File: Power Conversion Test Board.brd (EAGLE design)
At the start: 136.7 x 125.3 mm, 48 parts, among them U1 LM2678, U2 LM2678

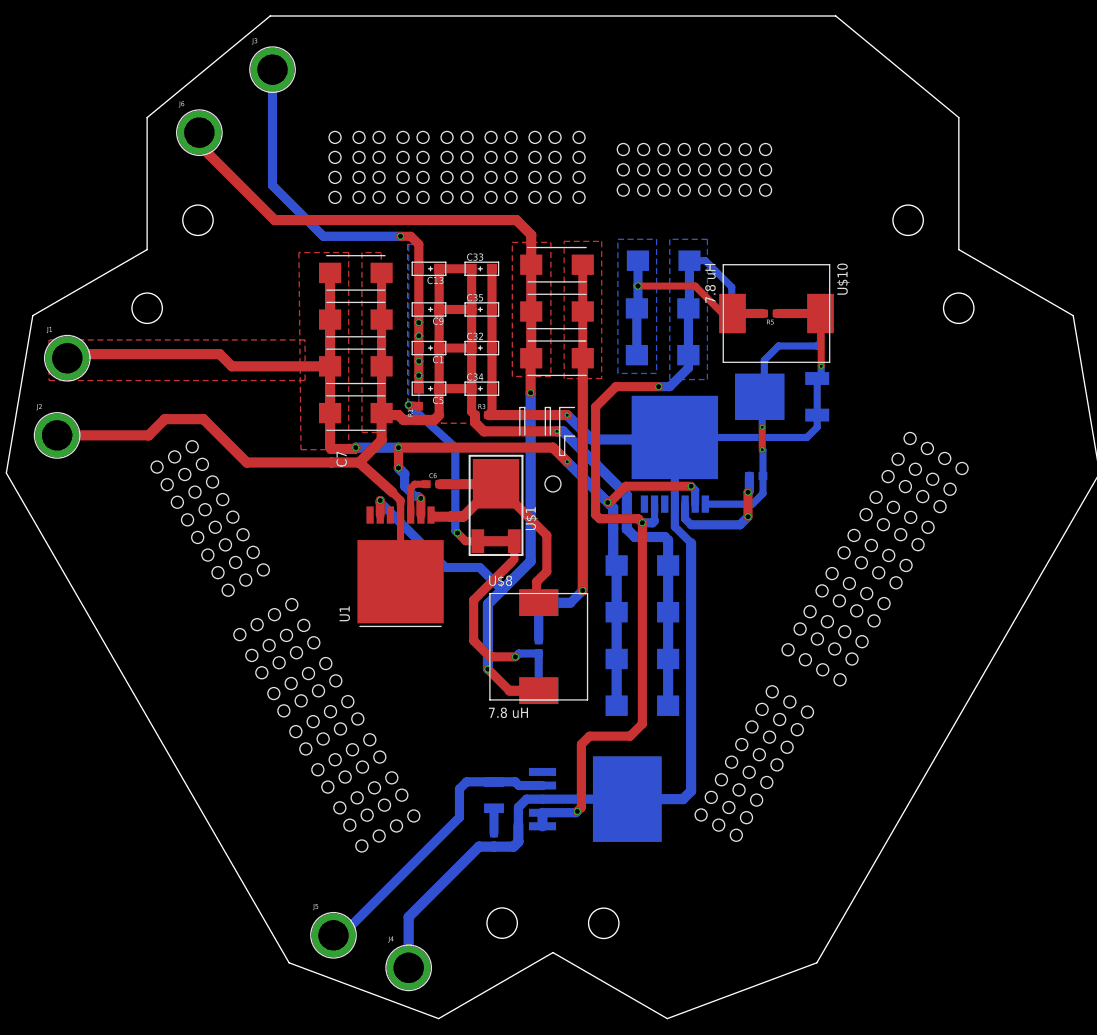
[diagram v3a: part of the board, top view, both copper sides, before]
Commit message: Added connectors
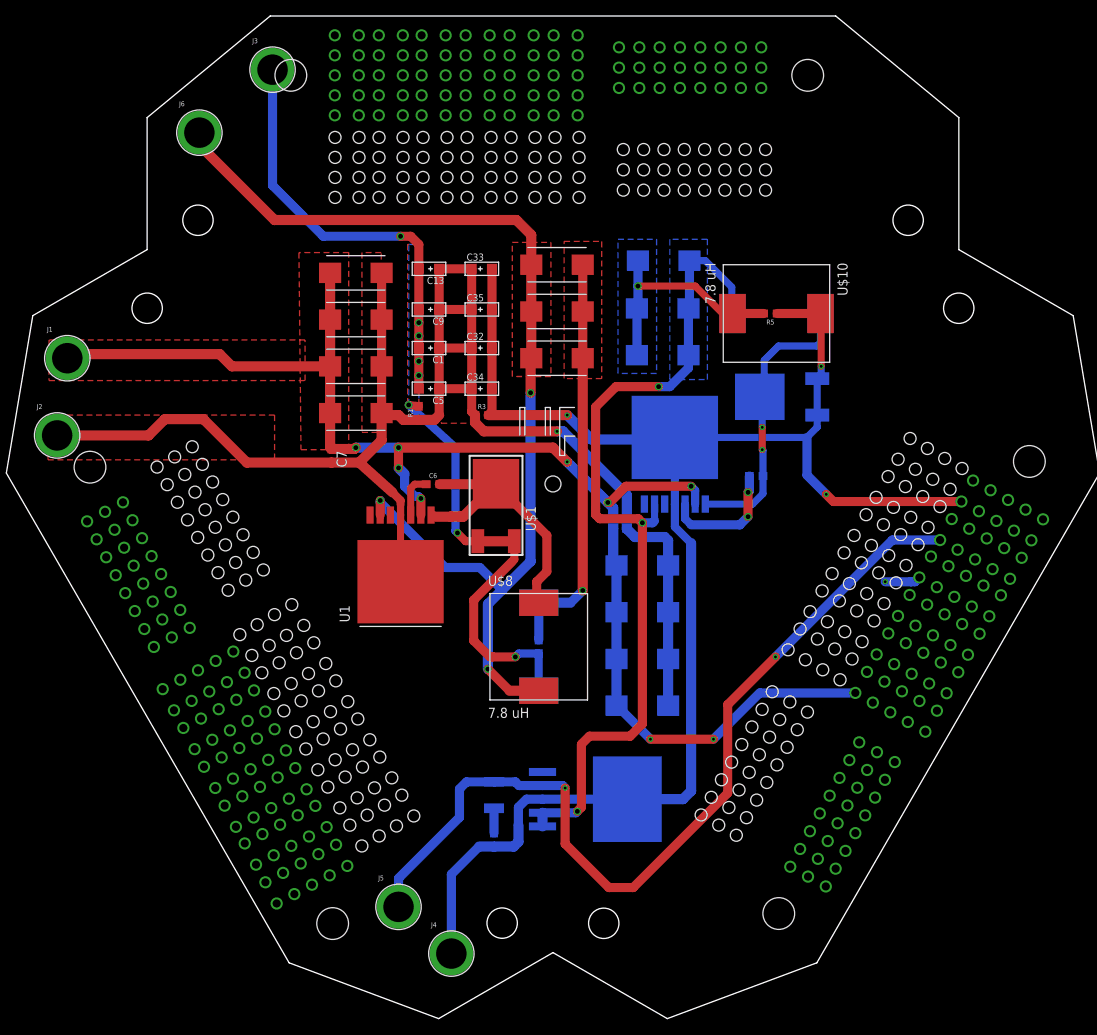
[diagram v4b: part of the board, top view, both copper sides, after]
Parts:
- added U$11, U$2, U$6: ET60T_2, ET60T:ET60T_2
- moved J5 8.87 mm to (-100.8, 15.2)
- moved J4 5.62 mm to (-94.2, 9.40)
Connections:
- new net +3.3VGND: U$6.R5-1, U$6.R5-10, U$6.R5-2, U$6.R5-3, U$6.R5-4, U$6.R5-5, U$6.R5-6, U$6.R5-7, U$6.R5-8, U$6.R5-9
- net +12V: now also U$11.R1-1, U$11.R1-10, U$11.R1-2, U$11.R1-3, U$11.R1-4, U$11.R1-5, U$11.R1-6, U$11.R1-7, U$11.R1-8, U$11.R1-9, U$2.R1-1, U$2.R1-10, U$2.R1-2, U$2.R1-3, U$2.R1-4, U$2.R1-5, U$2.R1-6, U$2.R1-7, U$2.R1-8, U$2.R1-9, U$6.R1-1, U$6.R1-10, U$6.R1-2, U$6.R1-3, U$6.R1-4, U$6.R1-5, U$6.R1-6, U$6.R1-7, U$6.R1-8, U$6.R1-9
- net +3.3V: now also U$11.R5-1, U$11.R5-10, U$11.R5-2, U$11.R5-3, U$11.R5-4, U$11.R5-5, U$11.R5-6, U$11.R5-7, U$11.R5-8, U$11.R5-9, U$2.R5-1, U$2.R5-10, U$2.R5-2, U$2.R5-3, U$2.R5-4, U$2.R5-5, U$2.R5-6, U$2.R5-7, U$2.R5-8, U$2.R5-9
- net +5V: now also U$11.R3-1, U$11.R3-10, U$11.R3-2, U$11.R3-3, U$11.R3-4, U$11.R3-5, U$11.R3-6, U$11.R3-7, U$11.R3-8, U$11.R3-9, U$2.R3-1, U$2.R3-10, U$2.R3-2, U$2.R3-3, U$2.R3-4, U$2.R3-5, U$2.R3-6, U$2.R3-7, U$2.R3-8, U$2.R3-9, U$6.R3-1, U$6.R3-10, U$6.R3-2, U$6.R3-3, U$6.R3-4, U$6.R3-5, U$6.R3-6, U$6.R3-7, U$6.R3-8, U$6.R3-9
- net 12VGND: now also U$11.R2-1, U$11.R2-10, U$11.R2-2, U$11.R2-3, U$11.R2-4, U$11.R2-5, U$11.R2-6, U$11.R2-7, U$11.R2-8, U$11.R2-9, U$2.R2-1, U$2.R2-10, U$2.R2-2, U$2.R2-3, U$2.R2-4, U$2.R2-5, U$2.R2-6, U$2.R2-7, U$2.R2-8, U$2.R2-9, U$6.R2-1, U$6.R2-10, U$6.R2-2, U$6.R2-3, U$6.R2-4, U$6.R2-5, U$6.R2-6, U$6.R2-7, U$6.R2-8, U$6.R2-9
- net 3.3VGND: now also U$11.R6-1, U$11.R6-10, U$11.R6-2, U$11.R6-3, U$11.R6-4, U$11.R6-5, U$11.R6-6, U$11.R6-7, U$11.R6-8, U$11.R6-9, U$2.R6-1, U$2.R6-10, U$2.R6-2, U$2.R6-3, U$2.R6-4, U$2.R6-5, U$2.R6-6, U$2.R6-7, U$2.R6-8, U$2.R6-9, U$6.R6-1, U$6.R6-10, U$6.R6-2, U$6.R6-3, U$6.R6-4, U$6.R6-5, U$6.R6-6, U$6.R6-7, U$6.R6-8, U$6.R6-9
- net 5VGND: now also U$11.R4-1, U$11.R4-10, U$11.R4-2, U$11.R4-3, U$11.R4-4, U$11.R4-5, U$11.R4-6, U$11.R4-7, U$11.R4-8, U$11.R4-9, U$2.R4-1, U$2.R4-10, U$2.R4-2, U$2.R4-3, U$2.R4-4, U$2.R4-5, U$2.R4-6, U$2.R4-7, U$2.R4-8, U$2.R4-9, U$6.R4-1, U$6.R4-10, U$6.R4-2, U$6.R4-3, U$6.R4-4, U$6.R4-5, U$6.R4-6, U$6.R4-7, U$6.R4-8, U$6.R4-9
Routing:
- net +3.3V: track 36.3 -> 112.4 mm, vias 0 -> 2
- net +12V: track 142.7 -> 176.6 mm, vias 7 -> 9
- net 3.3VGND: track 176.9 -> 198.3 mm, vias 2 -> 3
- net 5VGND: track 109.7 -> 114.2 mm, vias 8 -> 9

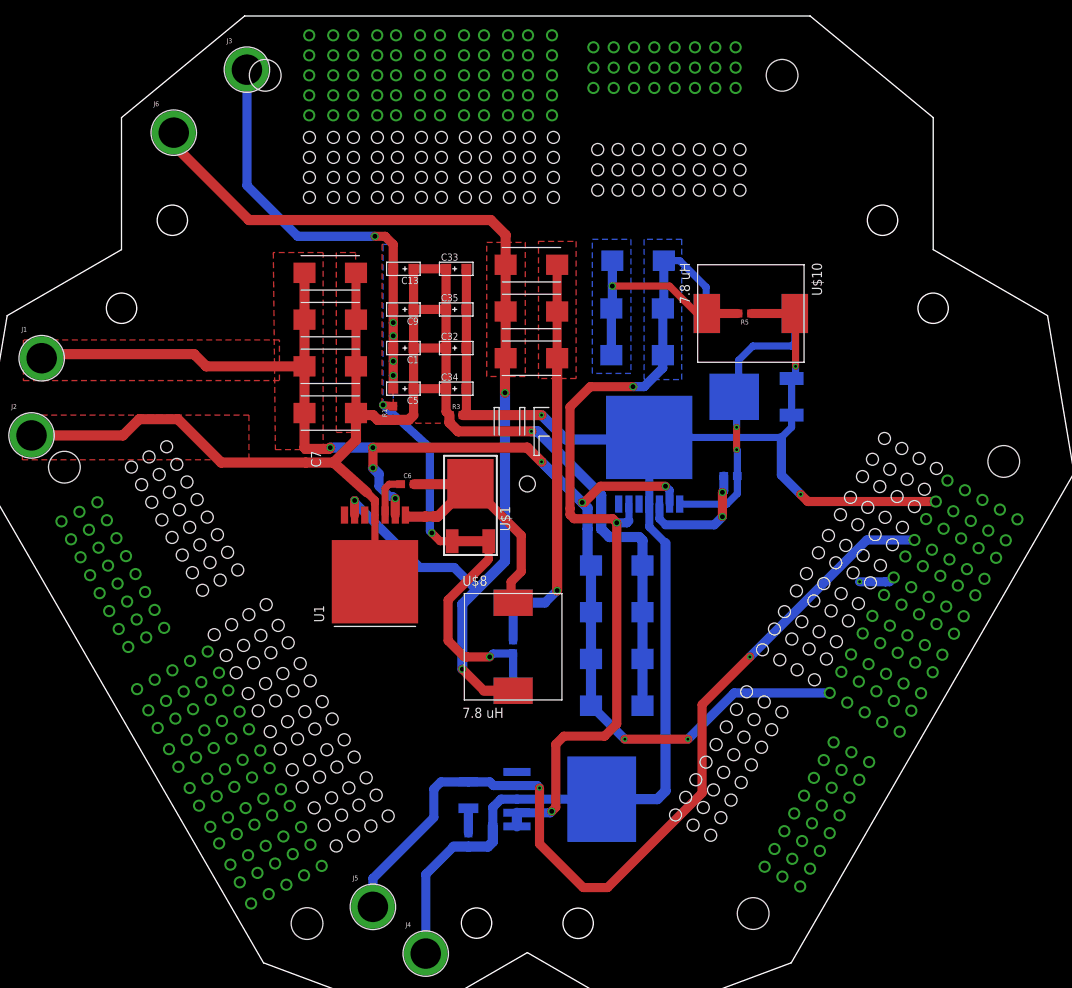
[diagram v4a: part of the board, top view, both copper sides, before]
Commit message: moved connectors
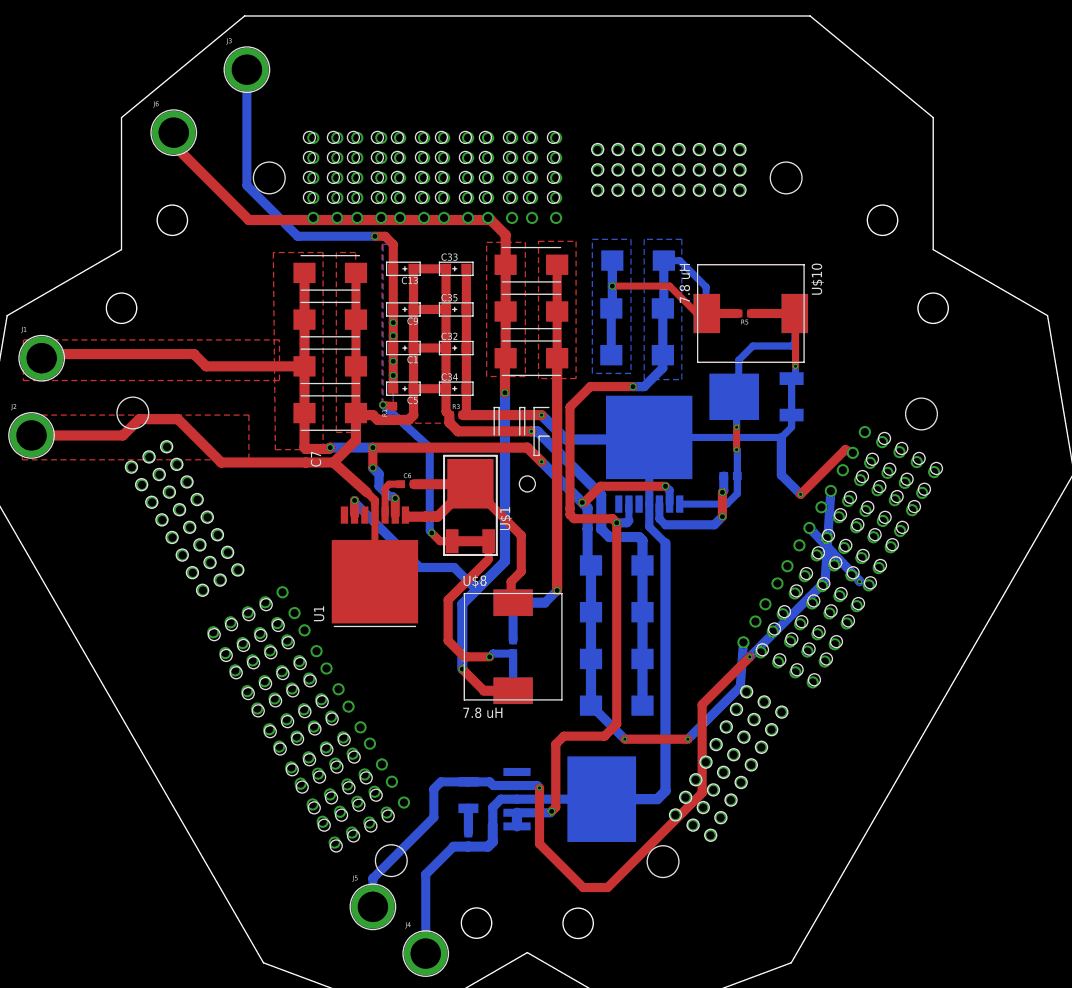
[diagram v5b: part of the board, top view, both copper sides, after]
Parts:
- moved U$6 12.8 mm to (-63.9, 107.3)
- moved U$2 12.7 mm to (-56.4, 33.1), turned to 60 degrees
- moved U$11 11.4 mm to (-124.3, 63.8), turned to 300 degrees
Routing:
- net 3.3VGND: track 198.3 -> 189.9 mm
- net +12V: track 176.6 -> 171.3 mm
- net 5VGND: track 114.2 -> 118.9 mm
- net +3.3V: track 112.4 -> 110.4 mm

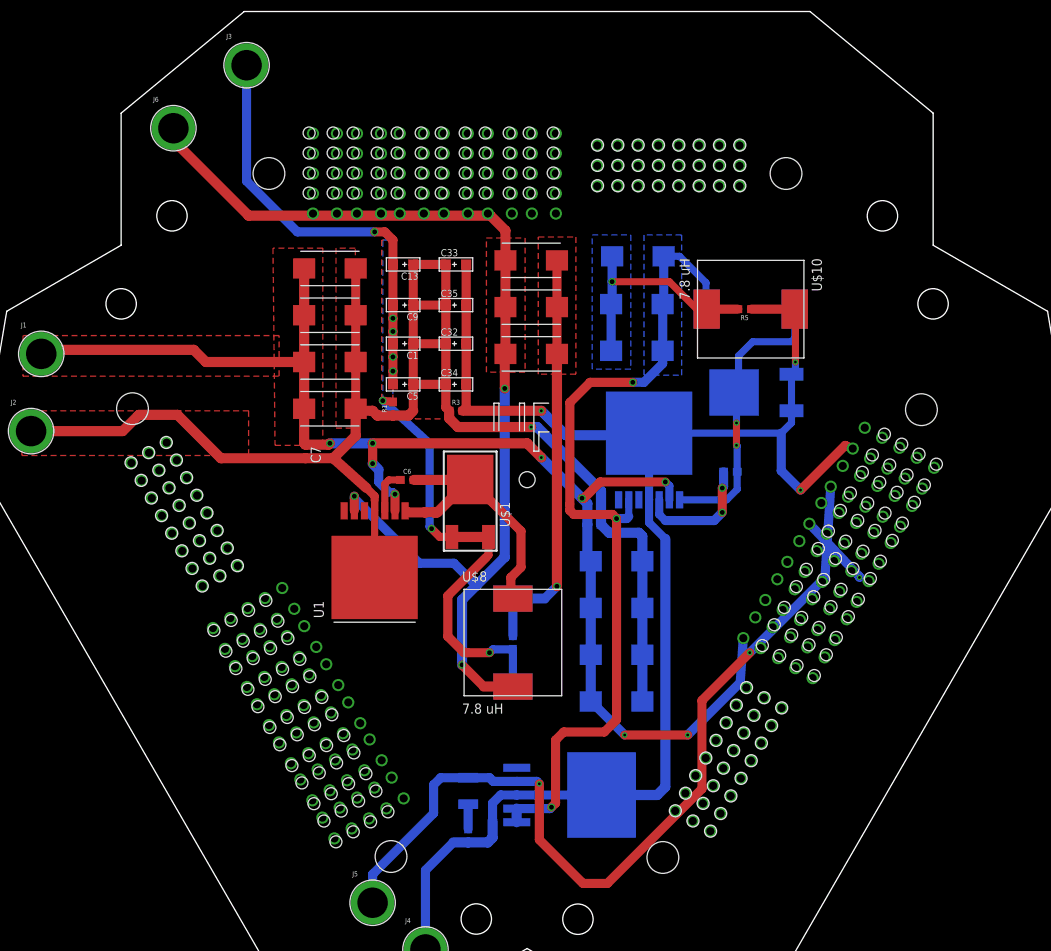
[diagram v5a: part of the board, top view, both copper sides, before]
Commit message: added connectors
the ones that go to distribution
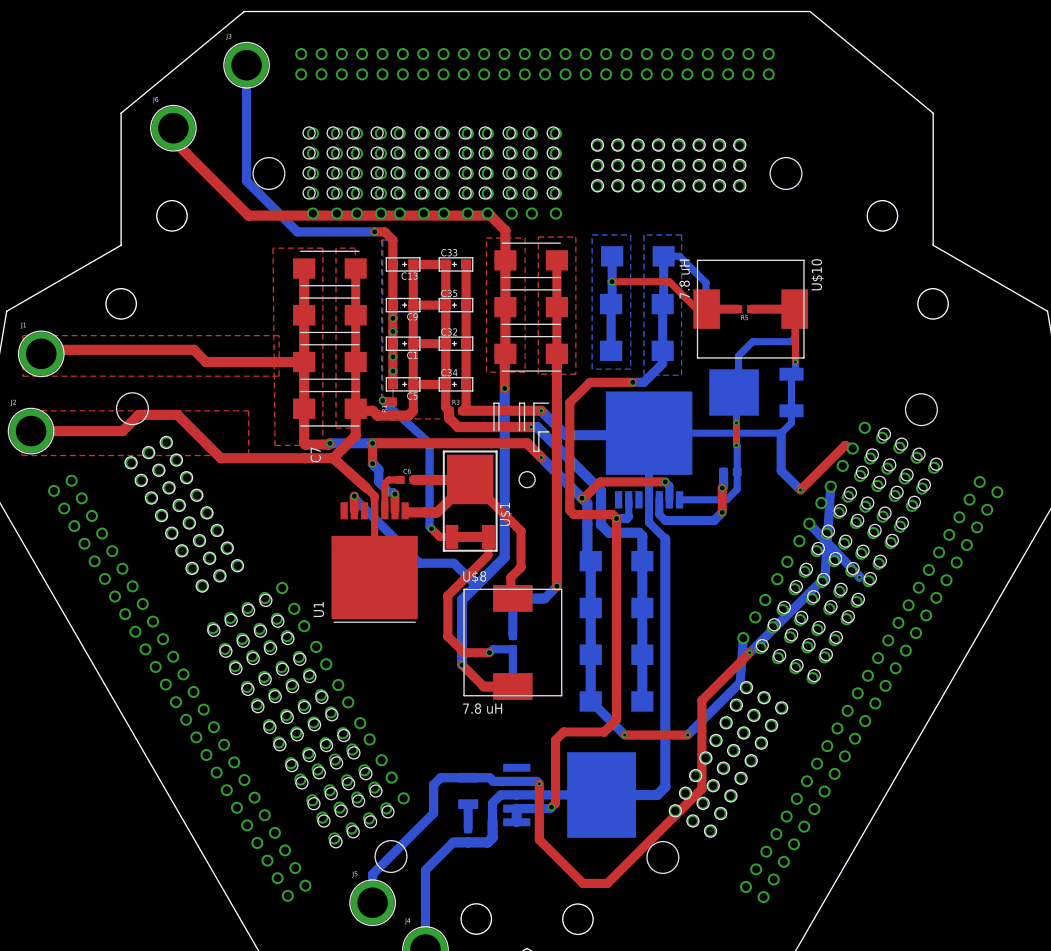
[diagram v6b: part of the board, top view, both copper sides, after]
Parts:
- added U$12, U$13, U$14: PDB_PCB_CONNEC, PDB_PCB_connectors:PDB_PCB
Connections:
- new net GND: U$12.GND10, U$12.GND11, U$12.GND12, U$12.GND13, U$12.GND14, U$12.GND15, U$12.GND16, U$12.GND17, U$12.GND18, U$12.GND19, U$12.GND2, U$12.GND20, U$12.GND21, U$12.GND22, U$12.GND23, U$12.GND24, U$12.GND3, U$12.GND4, U$12.GND5, U$12.GND6, U$12.GND7, U$12.GND8, U$12.GND9, U$13.GND10, U$13.GND11, U$13.GND12, U$13.GND13, U$13.GND14, U$13.GND15, U$13.GND16, U$13.GND17, U$13.GND18, U$13.GND19, U$13.GND2, U$13.GND20, U$13.GND21, U$13.GND22, U$13.GND23, U$13.GND24, U$13.GND3, U$13.GND4, U$13.GND5, U$13.GND6, U$13.GND7, U$13.GND8, U$13.GND9, U$14.GND10, U$14.GND11, U$14.GND12, U$14.GND13, U$14.GND14, U$14.GND15, U$14.GND16, U$14.GND17, U$14.GND18, U$14.GND19, U$14.GND2, U$14.GND20, U$14.GND21, U$14.GND22, U$14.GND23, U$14.GND24, U$14.GND3, U$14.GND4, U$14.GND5, U$14.GND6, U$14.GND7, U$14.GND8, U$14.GND9
- net +12V: now also U$12.+12V1, U$12.+12V10, U$12.+12V11, U$12.+12V12, U$12.+12V13, U$12.+12V14, U$12.+12V15, U$12.+12V16, U$12.+12V17, U$12.+12V18, U$12.+12V19, U$12.+12V2, U$12.+12V20, U$12.+12V21, U$12.+12V22, U$12.+12V23, U$12.+12V24, U$12.+12V3, U$12.+12V4, U$12.+12V5, U$12.+12V6, U$12.+12V7, U$12.+12V8, U$12.+12V9, U$13.+12V1, U$13.+12V10, U$13.+12V11, U$13.+12V12, U$13.+12V13, U$13.+12V14, U$13.+12V15, U$13.+12V16, U$13.+12V17, U$13.+12V18, U$13.+12V19, U$13.+12V2, U$13.+12V20, U$13.+12V21, U$13.+12V22, U$13.+12V23, U$13.+12V24, U$13.+12V3, U$13.+12V4, U$13.+12V5, U$13.+12V6, U$13.+12V7, U$13.+12V8, U$13.+12V9, U$14.+12V1, U$14.+12V10, U$14.+12V11, U$14.+12V12, U$14.+12V13, U$14.+12V14, U$14.+12V15, U$14.+12V16, U$14.+12V17, U$14.+12V18, U$14.+12V19, U$14.+12V2, U$14.+12V20, U$14.+12V21, U$14.+12V22, U$14.+12V23, U$14.+12V24, U$14.+12V3, U$14.+12V4, U$14.+12V5, U$14.+12V6, U$14.+12V7, U$14.+12V8, U$14.+12V9

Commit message: moved board to origin
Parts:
- removed U$11, U$2, U$6: ET60T_2, ET60T:ET60T_2
- moved C1 149.9 mm to (52.8, 83.8)
- moved C10 149.9 mm to (68.8, 94.2)
- moved C11 149.9 mm to (68.8, 88.4)
- moved C12 149.9 mm to (68.8, 82.5)
- moved C13 149.9 mm to (52.8, 93.7)
- moved C14 149.9 mm to (79.5, 39.1)
- moved C15 149.9 mm to (43.7, 93.2)
- moved C16 149.9 mm to (43.7, 87.4)
- moved C17 149.9 mm to (43.7, 81.5)
- moved C18 149.9 mm to (43.7, 75.7)
- moved C20 149.9 mm to (93.7, 67.8)
- moved C24 149.9 mm to (82.2, 94.7)
- moved C25 149.9 mm to (82.0, 88.8)
- moved C26 149.9 mm to (82.0, 82.9)
- moved C28 149.9 mm to (61.0, 27.9)
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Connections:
- removed net +3.3VGND: U$6.R5-1, U$6.R5-10, U$6.R5-2, U$6.R5-3, U$6.R5-4, U$6.R5-5, U$6.R5-6, U$6.R5-7, U$6.R5-8, U$6.R5-9
- net +12V: no longer U$11.R1-1, U$11.R1-10, U$11.R1-2, U$11.R1-3, U$11.R1-4, U$11.R1-5, U$11.R1-6, U$11.R1-7, U$11.R1-8, U$11.R1-9, U$2.R1-1, U$2.R1-10, U$2.R1-2, U$2.R1-3, U$2.R1-4, U$2.R1-5, U$2.R1-6, U$2.R1-7, U$2.R1-8, U$2.R1-9, U$6.R1-1, U$6.R1-10, U$6.R1-2, U$6.R1-3, U$6.R1-4, U$6.R1-5, U$6.R1-6, U$6.R1-7, U$6.R1-8, U$6.R1-9
- net +3.3V: no longer U$11.R5-1, U$11.R5-10, U$11.R5-2, U$11.R5-3, U$11.R5-4, U$11.R5-5, U$11.R5-6, U$11.R5-7, U$11.R5-8, U$11.R5-9, U$2.R5-1, U$2.R5-10, U$2.R5-2, U$2.R5-3, U$2.R5-4, U$2.R5-5, U$2.R5-6, U$2.R5-7, U$2.R5-8, U$2.R5-9
- net +5V: no longer U$11.R3-1, U$11.R3-10, U$11.R3-2, U$11.R3-3, U$11.R3-4, U$11.R3-5, U$11.R3-6, U$11.R3-7, U$11.R3-8, U$11.R3-9, U$2.R3-1, U$2.R3-10, U$2.R3-2, U$2.R3-3, U$2.R3-4, U$2.R3-5, U$2.R3-6, U$2.R3-7, U$2.R3-8, U$2.R3-9, U$6.R3-1, U$6.R3-10, U$6.R3-2, U$6.R3-3, U$6.R3-4, U$6.R3-5, U$6.R3-6, U$6.R3-7, U$6.R3-8, U$6.R3-9
- net 12VGND: no longer U$11.R2-1, U$11.R2-10, U$11.R2-2, U$11.R2-3, U$11.R2-4, U$11.R2-5, U$11.R2-6, U$11.R2-7, U$11.R2-8, U$11.R2-9, U$2.R2-1, U$2.R2-10, U$2.R2-2, U$2.R2-3, U$2.R2-4, U$2.R2-5, U$2.R2-6, U$2.R2-7, U$2.R2-8, U$2.R2-9, U$6.R2-1, U$6.R2-10, U$6.R2-2, U$6.R2-3, U$6.R2-4, U$6.R2-5, U$6.R2-6, U$6.R2-7, U$6.R2-8, U$6.R2-9
- net 3.3VGND: no longer U$11.R6-1, U$11.R6-10, U$11.R6-2, U$11.R6-3, U$11.R6-4, U$11.R6-5, U$11.R6-6, U$11.R6-7, U$11.R6-8, U$11.R6-9, U$2.R6-1, U$2.R6-10, U$2.R6-2, U$2.R6-3, U$2.R6-4, U$2.R6-5, U$2.R6-6, U$2.R6-7, U$2.R6-8, U$2.R6-9, U$6.R6-1, U$6.R6-10, U$6.R6-2, U$6.R6-3, U$6.R6-4, U$6.R6-5, U$6.R6-6, U$6.R6-7, U$6.R6-8, U$6.R6-9
- net 5VGND: no longer U$11.R4-1, U$11.R4-10, U$11.R4-2, U$11.R4-3, U$11.R4-4, U$11.R4-5, U$11.R4-6, U$11.R4-7, U$11.R4-8, U$11.R4-9, U$2.R4-1, U$2.R4-10, U$2.R4-2, U$2.R4-3, U$2.R4-4, U$2.R4-5, U$2.R4-6, U$2.R4-7, U$2.R4-8, U$2.R4-9, U$6.R4-1, U$6.R4-10, U$6.R4-2, U$6.R4-3, U$6.R4-4, U$6.R4-5, U$6.R4-6, U$6.R4-7, U$6.R4-8, U$6.R4-9
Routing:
- net 5VGND: track 118.9 -> 109.7 mm, vias 9 -> 8
- net +12V: track 171.3 -> 165.8 mm
- net 3.3VGND: track 189.9 -> 188.9 mm

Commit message: Did stuff and corrected stuff
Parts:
- added U$11, U$2, U$6: ET60S, ET60S:ET60S
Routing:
- net +3.3V: track 110.4 -> 38.8 mm, vias 2 -> 1
- net +12V: track 165.8 -> 156.5 mm
